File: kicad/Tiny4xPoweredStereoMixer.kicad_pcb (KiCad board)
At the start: 4 copper layers, 99.1 x 56.5 mm, 58 parts, among them J1 AudioJack3_SwitchTR, J2 AudioJack3_SwitchTR, J3 AudioJack3_SwitchTR, J4 AudioJack3_SwitchTR, J6 PowerConnector, J7 PowerConnector, J8 PowerConnector, J9 AudioJack3_SwitchTR, U1 TL072, U2 TL072, U6 LM2611AMF/NOPB

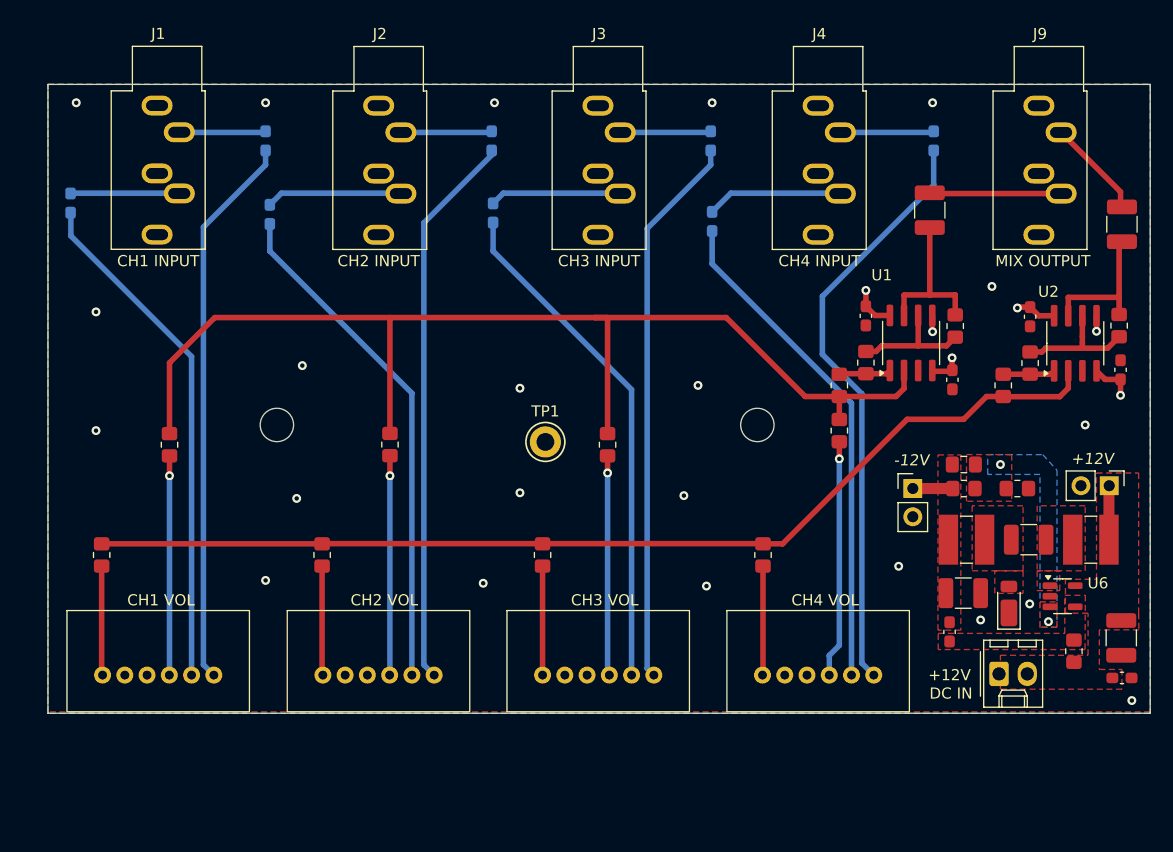
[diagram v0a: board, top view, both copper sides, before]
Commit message: updated schematic to use TPS54202
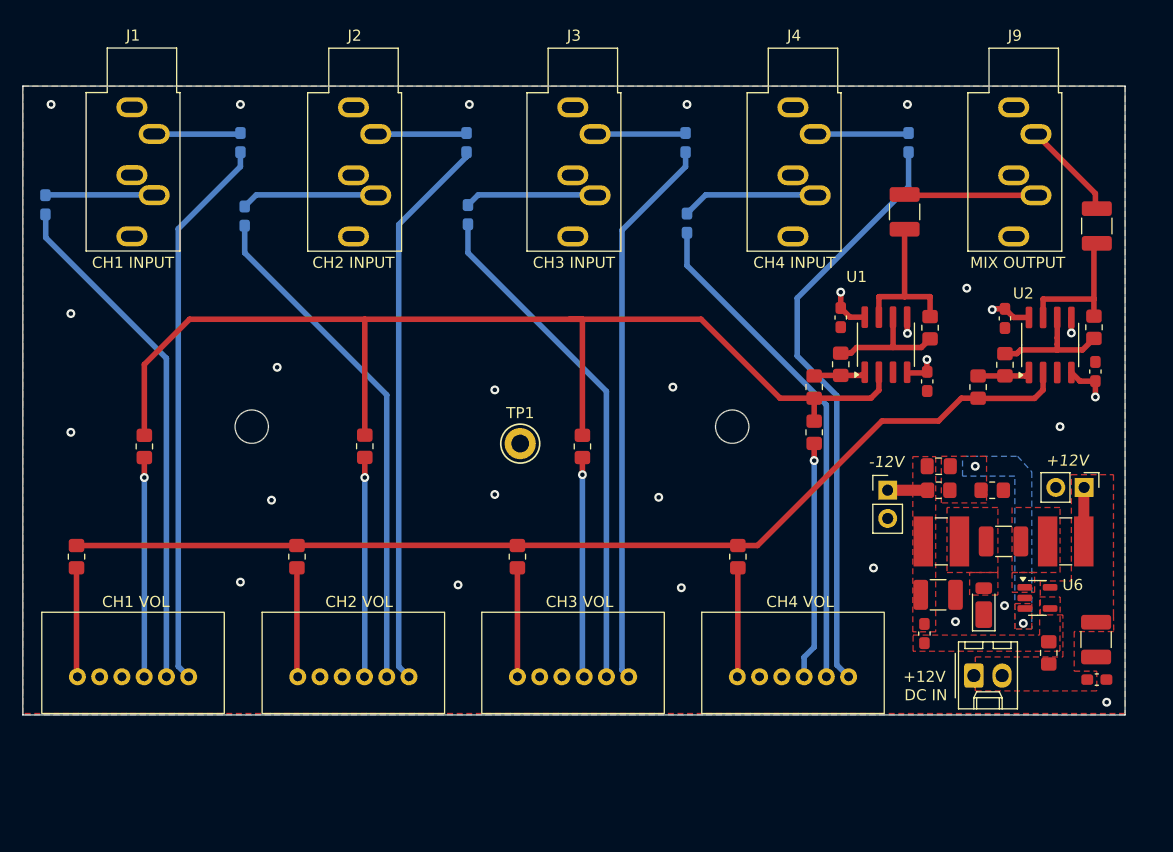
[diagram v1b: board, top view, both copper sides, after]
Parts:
- moved C1 2.27 mm to (198.1, 100.6)
- moved C10 2.27 mm to (141.5, 55.9)
- moved C12 2.27 mm to (161.2, 55.9)
- moved C13 2.27 mm to (189.9, 71.7)
- moved C15 2.27 mm to (198.1, 104.2)
- moved C16 2.27 mm to (182.7, 100.0)
- moved C19 2.27 mm to (198.1, 63.4)
- moved C2 2.27 mm to (189.8, 91.7)
- moved C6 2.27 mm to (182.9, 77.4)
- moved C7 2.27 mm to (103.7, 61.5)
- moved C9 2.27 mm to (175.1, 71.6)
- moved J2 2.27 mm to (131.3, 52.7)
- moved J3 2.27 mm to (151.1, 52.7)
- moved J4 2.27 mm to (170.8, 52.7)
- moved J6 2.27 mm to (187.1, 103.8)
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
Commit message: Set PCB rules and edded outline for Hammond RM2005S enclosure
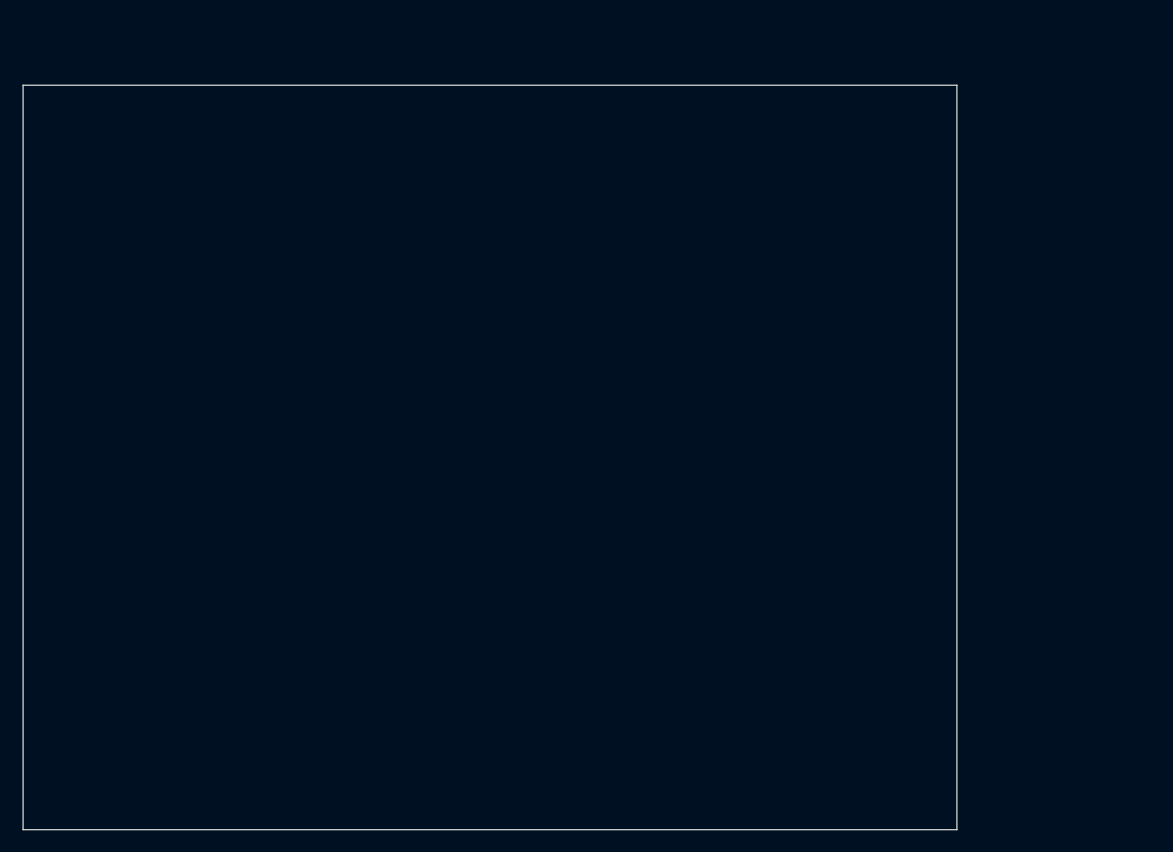
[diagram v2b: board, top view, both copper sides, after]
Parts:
- removed C1, C4: 22u, Capacitor_SMD:C_1210_3225Metric_Pad1.33x2.70mm_HandSolder
- removed C10, C11, C12, C13, C14, C15, C16, C17, C18, C5, C6, C7, C8, C9: 100nF, Capacitor_SMD:C_0603_1608Metric_Pad1.08x0.95mm_HandSolder
- removed C19, C20: 10uF, Capacitor_SMD:C_1210_3225Metric_Pad1.33x2.70mm_HandSolder
- removed C2: 2.2u, Capacitor_SMD:C_1210_3225Metric_Pad1.33x2.70mm_HandSolder
- removed C3: 1n, Capacitor_SMD:C_0805_2012Metric_Pad1.18x1.45mm_HandSolder
- removed D1: D_Schottky, Diode_SMD:D_PowerDI-123
- removed H1, H2: MountingHole, MountingHole:MountingHole_3mm
- removed J1, J2, J3, J4, J9: AudioJack3_SwitchTR, Connector_Audio:Jack_3.5mm_CUI_SJ1-3535NG_Horizontal
- removed J6: PowerConnector, Connector_Molex:Molex_KK-254_AE-6410-02A_1x02_P2.54mm_Vertical
- removed J7, J8: PowerConnector, Connector_PinHeader_2.54mm:PinHeader_1x02_P2.54mm_Vertical
- removed L1, L2: 22u, Inductor_SMD:L_Ferrocore_DLG-0403
- removed R1, R10, R12, R13, R14, R15, R2, R3, R4, R5, R6, R7, R8, R9: 10k, Resistor_SMD:R_0805_2012Metric_Pad1.20x1.40mm_HandSolder
- removed R11: 100k, Resistor_SMD:R_0805_2012Metric_Pad1.20x1.40mm_HandSolder
- removed RFB1: 22k, Resistor_SMD:R_0805_2012Metric_Pad1.20x1.40mm_HandSolder
- removed RFB2: 2k2, Resistor_SMD:R_0805_2012Metric_Pad1.20x1.40mm_HandSolder
- removed RV1, RV2, RV3, RV4: 10k, Potentiometers:Alps_RK12L12_Double_Horizontal
- removed TP1: TestPoint, TestPoint:TestPoint_Keystone_5005-5009_Compact
- removed U1, U2: TL072, Package_SO:SOIC-8_3.9x4.9mm_P1.27mm
- removed U6: LM2611AMF/NOPB, Package_TO_SOT_SMD:SOT-23-5
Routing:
- net Net-(U1A--): track 103.0 -> 0.00 mm
- net Net-(U2A--): track 94.3 -> 0.00 mm
- net Net-(C17-Pad2): track 53.2 -> 0.00 mm
- net Net-(C10-Pad2): track 50.1 -> 0.00 mm
- net Net-(C5-Pad2): track 49.8 -> 0.00 mm
- net Net-(C12-Pad2): track 49.8 -> 0.00 mm
- net Net-(C7-Pad2): track 46.1 -> 0.00 mm
- net Net-(C11-Pad2): track 45.8 -> 0.00 mm
- net Net-(C14-Pad2): track 45.8 -> 0.00 mm
- net Net-(C18-Pad2): track 45.1 -> 0.00 mm
- net /ch4_right_mix_in: track 21.3 -> 0.00 mm, vias 1 -> 0
- net /ch3_right_mix_in: track 19.8 -> 0.00 mm, vias 1 -> 0
- net /ch2_right_mix_in: track 19.7 -> 0.00 mm, vias 1 -> 0
- net /ch1_right_mix_in: track 19.7 -> 0.00 mm, vias 1 -> 0
- net Net-(C20-Pad1): track 14.3 -> 0.00 mm
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- removed copper zone on In1.Cu, net +12V
- removed copper zone on In2.Cu, net -12V
- removed copper zone on B.Cu, net GND
- removed copper zone on F.Cu, net GND
- removed copper zone on F.Cu, net Net-(D1-A)
- removed copper zone on F.Cu, net Net-(J6-Pin_2)
- removed copper zone on F.Cu, net Net-(J8-Pin_1)
- removed copper zone on B.Cu, net Net-(U6-NFB)
- removed copper zone on F.Cu, net Net-(U6-NFB)
- removed copper zone on F.Cu, net Net-(U6-SW)
- removed copper zone on F.Cu, net Net-(U6-~{SHDN})
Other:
- board size 99.1 x 56.5 mm -> 83.9 x 66.9 mm
- board text added: "Enclosure: https://www.hammfg.com/files/parts/pdf/RM2005S.pdf"
- board text removed: "Tiny 4-Channel Active Stereo Mixer Rev${REVISION} ${ISSUE_DATE}"

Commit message: Finished RevC layout
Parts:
- added C1: 10uF, Capacitor_SMD:C_0805_2012Metric_Pad1.18x1.45mm_HandSolder, F.Cu at (179.1, 80.0)
- added C10: 100nF, Capacitor_SMD:C_0603_1608Metric_Pad1.08x0.95mm_HandSolder, B.Cu at (136.7, 54.9)
- added C11: 100nF, Capacitor_SMD:C_0603_1608Metric_Pad1.08x0.95mm_HandSolder, B.Cu at (136.7, 60.3)
- added C12: 100nF, Capacitor_SMD:C_0603_1608Metric_Pad1.08x0.95mm_HandSolder, B.Cu at (150.9, 54.9)
- added C13: 100nF, Capacitor_SMD:C_0603_1608Metric_Pad1.08x0.95mm_HandSolder, F.Cu at (140.3, 76.8)
- added C14: 100nF, Capacitor_SMD:C_0603_1608Metric_Pad1.08x0.95mm_HandSolder, B.Cu at (150.9, 60.3)
- added C15: 10uF, Capacitor_SMD:C_0805_2012Metric_Pad1.18x1.45mm_HandSolder, B.Cu at (169.0, 82.5)
- added C16: 100nF, Capacitor_SMD:C_0805_2012Metric_Pad1.18x1.45mm_HandSolder, B.Cu at (165.4, 78.9)
- added C17: 100nF, Capacitor_SMD:C_0603_1608Metric_Pad1.08x0.95mm_HandSolder, B.Cu at (165.6, 54.9)
- added C18: 100nF, Capacitor_SMD:C_0603_1608Metric_Pad1.08x0.95mm_HandSolder, B.Cu at (165.6, 60.3)
- added C19: 10uF, Capacitor_SMD:C_0805_2012Metric_Pad1.18x1.45mm_HandSolder, F.Cu at (122.2, 79.6)
- added C2: 10uF, Capacitor_SMD:C_0805_2012Metric_Pad1.18x1.45mm_HandSolder, F.Cu at (179.1, 82.6)
- added C20: 10uF, Capacitor_SMD:C_0805_2012Metric_Pad1.18x1.45mm_HandSolder, F.Cu at (146.6, 79.4)
- added C21: 100nF, Capacitor_SMD:C_0805_2012Metric_Pad1.18x1.45mm_HandSolder, F.Cu at (160.3, 85.1)
- added C22: 22uF, Capacitor_SMD:C_0805_2012Metric_Pad1.18x1.45mm_HandSolder, F.Cu at (160.3, 87.6)
- added C23: 22uF, Capacitor_SMD:C_0805_2012Metric_Pad1.18x1.45mm_HandSolder, F.Cu at (160.3, 74.9)
- added C24: 22uF, Capacitor_SMD:C_0805_2012Metric_Pad1.18x1.45mm_HandSolder, F.Cu at (160.3, 77.4)
- added C25: 22uF, Capacitor_SMD:C_0805_2012Metric_Pad1.18x1.45mm_HandSolder, F.Cu at (160.3, 80.0)
- added C26: 22uF, Capacitor_SMD:C_0805_2012Metric_Pad1.18x1.45mm_HandSolder, F.Cu at (160.3, 82.5)
- added C3: 100nF, Capacitor_SMD:C_0805_2012Metric_Pad1.18x1.45mm_HandSolder, F.Cu at (179.1, 85.1)
- added C4: 100nF, Capacitor_SMD:C_0805_2012Metric_Pad1.18x1.45mm_HandSolder, B.Cu at (169.0, 85.1)
- added C5: 100nF, Capacitor_SMD:C_0603_1608Metric_Pad1.08x0.95mm_HandSolder, B.Cu at (121.9, 54.9)
- added C6: 100nF, Capacitor_SMD:C_0603_1608Metric_Pad1.08x0.95mm_HandSolder, F.Cu at (112.0, 87.4)
- added C7: 100nF, Capacitor_SMD:C_0603_1608Metric_Pad1.08x0.95mm_HandSolder, B.Cu at (121.9, 60.3)
- added C8: 100nF, Capacitor_SMD:C_0603_1608Metric_Pad1.08x0.95mm_HandSolder, F.Cu at (136.6, 87.4)
- added C9: 100nF, Capacitor_SMD:C_0603_1608Metric_Pad1.08x0.95mm_HandSolder, F.Cu at (115.9, 76.8)
- added D1: LED, LED_SMD:LED_1206_3216Metric_Pad1.42x1.75mm_HandSolder, F.Cu at (159.8, 92.7)
- added H1: MountingHole, MountingHole:MountingHole_2.7mm_M2.5, F.Cu at (104.7, 67.0)
- added H2: MountingHole, MountingHole:MountingHole_2.7mm_M2.5, F.Cu at (182.6, 67.0)
- added H3: MountingHole, MountingHole:MountingHole_2.7mm_M2.5, F.Cu at (104.7, 101.0)
- added H4: MountingHole, MountingHole:MountingHole_2.7mm_M2.5, F.Cu at (182.6, 101.0)
- added J1: AudioJack3_SwitchTR, Connector_Audio:Jack_3.5mm_CUI_SJ1-3535NG_Horizontal, F.Cu at (114.6, 51.8)
- added J2: AudioJack3_SwitchTR, Connector_Audio:Jack_3.5mm_CUI_SJ1-3535NG_Horizontal, F.Cu at (129.1, 51.8)
- added J3: AudioJack3_SwitchTR, Connector_Audio:Jack_3.5mm_CUI_SJ1-3535NG_Horizontal, F.Cu at (143.6, 51.8)
- added J4: AudioJack3_SwitchTR, Connector_Audio:Jack_3.5mm_CUI_SJ1-3535NG_Horizontal, F.Cu at (158.1, 51.8)
- added J5: PowerConnector, Connector_Molex:Molex_KK-254_AE-6410-02A_1x02_P2.54mm_Vertical, F.Cu at (180.4, 90.3)
- added J9: AudioJack3_SwitchTR, Connector_Audio:Jack_3.5mm_CUI_SJ1-3535NG_Horizontal, F.Cu at (172.5, 51.8)
- added L1: 22uH, Inductor_SMD:L_Ferrocore_DLG-0403, F.Cu at (168.9, 90.3)
- added R1: 10k, Resistor_SMD:R_0805_2012Metric_Pad1.20x1.40mm_HandSolder, F.Cu at (168.7, 104.6)
- added R10: 10k, Resistor_SMD:R_0805_2012Metric_Pad1.20x1.40mm_HandSolder, F.Cu at (146.6, 83.2)
- added R12: 10k, Resistor_SMD:R_0805_2012Metric_Pad1.20x1.40mm_HandSolder, F.Cu at (141.0, 87.6)
- added R13: 10k, Resistor_SMD:R_0805_2012Metric_Pad1.20x1.40mm_HandSolder, F.Cu at (108.2, 82.1)
- added R14: 10k, Resistor_SMD:R_0805_2012Metric_Pad1.20x1.40mm_HandSolder, F.Cu at (116.2, 87.6)
- added R15: 10k, Resistor_SMD:R_0805_2012Metric_Pad1.20x1.40mm_HandSolder, F.Cu at (122.2, 83.4)
- added R18: 50K, Resistor_SMD:R_0805_2012Metric_Pad1.20x1.40mm_HandSolder, F.Cu at (179.1, 74.9)
- added R19: 2K4, Resistor_SMD:R_0805_2012Metric_Pad1.20x1.40mm_HandSolder, F.Cu at (169.0, 74.9)
- added R2: 10k, Resistor_SMD:R_0805_2012Metric_Pad1.20x1.40mm_HandSolder, F.Cu at (148.6, 104.6)
- added R20: 2K2, Resistor_SMD:R_0805_2012Metric_Pad1.20x1.40mm_HandSolder, F.Cu at (157.2, 90.2)
- added R3: 10k, Resistor_SMD:R_0805_2012Metric_Pad1.20x1.40mm_HandSolder, F.Cu at (128.5, 104.6)
- added R4: 10k, Resistor_SMD:R_0805_2012Metric_Pad1.20x1.40mm_HandSolder, F.Cu at (110.2, 104.6)
- added R5: 10k, Resistor_SMD:R_0805_2012Metric_Pad1.20x1.40mm_HandSolder, F.Cu at (174.8, 104.6)
- added R6: 10k, Resistor_SMD:R_0805_2012Metric_Pad1.20x1.40mm_HandSolder, F.Cu at (154.7, 104.6)
- added R7: 10k, Resistor_SMD:R_0805_2012Metric_Pad1.20x1.40mm_HandSolder, F.Cu at (134.6, 104.6)
- added R8: 10k, Resistor_SMD:R_0805_2012Metric_Pad1.20x1.40mm_HandSolder, F.Cu at (114.8, 104.6)
- added R9: 10k, Resistor_SMD:R_0805_2012Metric_Pad1.20x1.40mm_HandSolder, F.Cu at (132.6, 82.2)
- added RV1: 10k, Potentiometers:Alps_RK12L12_Double_Horizontal, F.Cu at (113.7, 110.5)
- added RV2: 10k, Potentiometers:Alps_RK12L12_Double_Horizontal, F.Cu at (133.6, 110.5)
- added RV3: 10k, Potentiometers:Alps_RK12L12_Double_Horizontal, F.Cu at (153.6, 110.5)
- added RV4: 10k, Potentiometers:Alps_RK12L12_Double_Horizontal, F.Cu at (173.6, 110.5)
- added U1: TL072, Package_SO:SOIC-8_3.9x4.9mm_P1.27mm, F.Cu at (139.0, 81.9)
- added U2: TL072, Package_SO:SOIC-8_3.9x4.9mm_P1.27mm, F.Cu at (114.6, 81.9)
- added U3: TPS54202DDC, Package_TO_SOT_SMD:SOT-23-6, F.Cu at (169.0, 78.9)
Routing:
- net Net-(U1A--): track 0.00 -> 101.6 mm, vias 0 -> 6
- net Net-(U2A--): track 0.00 -> 98.9 mm
- net Net-(C19-Pad2): track 0.00 -> 68.4 mm
- net Net-(C18-Pad2): track 0.00 -> 68.1 mm
- net Net-(C17-Pad2): track 0.00 -> 63.8 mm
- net Net-(C5-Pad2): track 0.00 -> 61.6 mm
- net Net-(C12-Pad2): track 0.00 -> 61.6 mm
- net Net-(C10-Pad2): track 0.00 -> 59.4 mm
- net Net-(C14-Pad2): track 0.00 -> 55.4 mm
- net Net-(C7-Pad2): track 0.00 -> 54.8 mm
- net Net-(C11-Pad2): track 0.00 -> 52.8 mm
- net Net-(C20-Pad2): track 0.00 -> 37.3 mm
- net -12V: track 0.00 -> 22.2 mm, vias 0 -> 4
- net +12V: track 0.00 -> 15.3 mm, vias 0 -> 4
- net Net-(R12-Pad1): track 0.00 -> 14.5 mm
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- added copper zone on F.Cu, net +12V
- added copper zone on In1.Cu, net +12V
- added copper zone on F.Cu, net -12V
- added copper zone on In2.Cu, net -12V
- added copper zone on B.Cu, net GND
- added copper zone on F.Cu, net GND
- added copper zone on F.Cu, net Net-(U3-SW)
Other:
- board size 83.9 x 66.9 mm -> 84 x 67.5 mm
- board text added: "${PROJECTNAME}"
- board text added: "Rev ${REVISION} ${WEEK}"

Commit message: rev c layout complete
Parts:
- moved J1 0.10 mm to (114.6, 51.9)
- moved J2 0.10 mm to (129.1, 51.9)
- moved J3 0.10 mm to (143.6, 51.9)
- moved J4 0.10 mm to (158.1, 51.9)
- moved J9 0.10 mm to (172.5, 51.9)
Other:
- board size 84 x 67.5 mm -> 84 x 67.2 mm
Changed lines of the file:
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@@
 	)
 	(footprint "Connector_Audio:Jack_3.5mm_CUI_SJ1-3535NG_Horizontal"
-		(locked yes)
 		(layer "F.Cu")
-		(at 114.6318 51.816)
+		(at 114.6318 51.9176)
 		(descr "TRS 3.5mm, horizontal, through-hole, with switch, https://www.cui.com/product/resource/sj1-353xng.pdf")
 		(tags "TRS audio jack stereo horizontal")
@@
 			(pintype "passive")
 		)
-		(model "${KICAD8_3DMODEL_DIR}/Connector_Audio.3dshapes/Jack_3.5mm_CUI_SJ1-3535NG_Horizontal.wrl"
+		(model "${KIPRJMOD}/Footprints/Same_Sky_SJ1-3535NG-BE.step"
 			(offset
-				(xyz 0 0 0)
+				(xyz 1 5.25 7)
 			)
 			(scale
@@
 			)
 			(rotate
-				(xyz 0 0 0)
+				(xyz 180 0 -90)
 			)
 		)
@@
 	)
 	(footprint "Connector_Audio:Jack_3.5mm_CUI_SJ1-3535NG_Horizontal"
-		(locked yes)
 		(layer "F.Cu")
-		(at 158.0658 51.816)
+		(at 158.0658 51.9176)
 		(descr "TRS 3.5mm, horizontal, through-hole, with switch, https://www.cui.com/product/resource/sj1-353xng.pdf")
 		(tags "TRS audio jack stereo horizontal")
@@
 			(pintype "passive")
 		)
-		(model "${KICAD8_3DMODEL_DIR}/Connector_Audio.3dshapes/Jack_3.5mm_CUI_SJ1-3535NG_Horizontal.wrl"
+		(model "${KIPRJMOD}/Footprints/Same_Sky_SJ1-3535NG-BE.step"
 			(offset
-				(xyz 0 0 0)
+				(xyz 1 5.25 7)
 			)
 			(scale
@@
 			)
 			(rotate
-				(xyz 0 0 0)
+				(xyz 180 0 -90)
 			)
 		)
@@
 	)
 	(footprint "Connector_Audio:Jack_3.5mm_CUI_SJ1-3535NG_Horizontal"
-		(locked yes)
 		(layer "F.Cu")
-		(at 143.5878 51.816)
+		(at 143.5878 51.9176)
 		(descr "TRS 3.5mm, horizontal, through-hole, with switch, https://www.cui.com/product/resource/sj1-353xng.pdf")
 		(tags "TRS audio jack stereo horizontal")
@@
 			(pintype "passive")
 		)
-		(model "${KICAD8_3DMODEL_DIR}/Connector_Audio.3dshapes/Jack_3.5mm_CUI_SJ1-3535NG_Horizontal.wrl"
+		(model "${KIPRJMOD}/Footprints/Same_Sky_SJ1-3535NG-BE.step"
 			(offset
-				(xyz 0 0 0)
+				(xyz 1 5.25 7.5)
 			)
 			(scale
@@
 			)
 			(rotate
-				(xyz 0 0 0)
+				(xyz 180 0 -90)
 			)
 		)
@@
 	)
 	(footprint "Potentiometers:Alps_RK12L12_Double_Horizontal"
-		(locked yes)
 		(layer "F.Cu")
 		(at 113.653 110.472)
@@
 	)
 	(footprint "Connector_Audio:Jack_3.5mm_CUI_SJ1-3535NG_Horizontal"
-		(locked yes)
 		(layer "F.Cu")
-		(at 172.5438 51.816)
+		(at 172.5438 51.9176)
 		(descr "TRS 3.5mm, horizontal, through-hole, with switch, https://www.cui.com/product/resource/sj1-353xng.pdf")
 		(tags "TRS audio jack stereo horizontal")
@@
 			(pintype "passive")
 		)
-		(model "${KICAD8_3DMODEL_DIR}/Connector_Audio.3dshapes/Jack_3.5mm_CUI_SJ1-3535NG_Horizontal.wrl"
+		(model "${KIPRJMOD}/Footprints/Same_Sky_SJ1-3535NG-BE.step"
 			(offset
-				(xyz 0 0 0)
+				(xyz 1 5.25 7)
 			)
 			(scale
@@
 			)
 			(rotate
-				(xyz 0 0 0)
+				(xyz 180 0 -90)
 			)
 		)
@@
 	)
 	(footprint "Connector_Audio:Jack_3.5mm_CUI_SJ1-3535NG_Horizontal"
-		(locked yes)
 		(layer "F.Cu")
-		(at 129.1098 51.816)
+		(at 129.1098 51.9176)
 		(descr "TRS 3.5mm, horizontal, through-hole, with switch, https://www.cui.com/product/resource/sj1-353xng.pdf")
 		(tags "TRS audio jack stereo horizontal")
@@
 			(pintype "passive")
 		)
-		(model "${KICAD8_3DMODEL_DIR}/Connector_Audio.3dshapes/Jack_3.5mm_CUI_SJ1-3535NG_Horizontal.wrl"
+		(model "${KIPRJMOD}/Footprints/Same_Sky_SJ1-3535NG-BE.step"
 			(offset
-				(xyz 0 0 0)
+				(xyz 1 5.25 7)
 			)
 			(scale
@@
 			)
 			(rotate
-				(xyz 0 0 0)
+				(xyz 180 0 -90)
 			)
 		)
 	)
 	(footprint "Potentiometers:Alps_RK12L12_Double_Horizontal"
-		(locked yes)
 		(layer "F.Cu")
 		(at 133.648066 110.472)
@@
 	)
 	(footprint "Potentiometers:Alps_RK12L12_Double_Horizontal"
-		(locked yes)
 		(layer "F.Cu")
 		(at 153.643132 110.472)
@@
 	)
 	(footprint "Potentiometers:Alps_RK12L12_Double_Horizontal"
-		(locked yes)
 		(layer "F.Cu")
 		(at 173.6382 110.472)
@@
 	(gr_line
 		(start 101.6508 117.6528)
-		(end 101.6508 50.1528)
-		(locked yes)
+		(end 101.6508 50.4444)
 		(stroke
 			(width 0.1)
@@
 	)
 	(gr_line
-		(start 101.6508 50.1528)
-		(end 185.6508 50.1528)
-		(locked yes)
+		(start 101.6508 50.4444)
+		(end 185.6508 50.4444)
 		(stroke
 			(width 0.1)
@@
 	)
 	(gr_line
-		(start 185.6508 50.1528)
+		(start 185.6508 50.4444)
 		(end 185.6508 117.6528)
-		(locked yes)
 		(stroke
 			(width 0.1)
@@
 		(layer "Edge.Cuts")
 	)
-	(gr_text "Enclosure:\nhttps://www.hammfg.com/files/parts/pdf/RM2005S.pdf"
-		(at 100.9904 126.0348 0)
-		(layer "Cmts.User")
-		(effects
-			(font
-				(size 1 1)
-				(thickness 0.15)
-			)
-			(justify left bottom)
-		)
-	)
 	(gr_text "${PROJECTNAME}\n"
-		(at 114.3 69.85 0)
-		(layer "Edge.Cuts")
+		(at 114.2492 69.7992 0)
+		(layer "F.SilkS")
 		(effects
 			(font
@@
 	(gr_text "Rev ${REVISION} ${WEEK}\n"
 		(at 114.3 71.755 0)
-		(layer "Edge.Cuts")
+		(layer "F.SilkS")
 		(effects
 			(font
@@
 		)
 	)
+	(gr_text "Enclosure:\nhttps://www.hammfg.com/files/parts/pdf/RM2005S.pdf"
+		(at 100.9904 126.0348 0)
+		(layer "Cmts.User")
+		(effects
+			(font
+				(size 1 1)
+				(thickness 0.15)
+			)
+			(justify left bottom)
+		)
+	)
 	(segment
 		(start 169.926 81.28)
@@
 		(polygon
 			(pts
-				(xy 101.6 50.165) (xy 185.674 50.165) (xy 185.674 117.6528) (xy 101.6508 117.6528)
+				(xy 101.6 50.5206) (xy 185.674 50.5206) (xy 185.674 117.6528) (xy 101.6508 117.6528)
 			)
 		)
@@
 		(polygon
 			(pts
-				(xy 101.6508 50.1396) (xy 185.6232 50.1396) (xy 185.674 117.6528) (xy 101.6508 117.6528)
+				(xy 101.6508 50.4952) (xy 185.6232 50.4952) (xy 185.674 117.6528) (xy 101.6508 117.6528)
 			)
 		)
@@
 		(polygon
 			(pts
-				(xy 101.6508 50.165) (xy 185.6486 50.165) (xy 185.6486 117.6528) (xy 101.6508 117.6528)
+				(xy 101.6508 50.5206) (xy 185.6486 50.4444) (xy 185.6486 117.6528) (xy 101.6508 117.6528)
 			)
 		)
